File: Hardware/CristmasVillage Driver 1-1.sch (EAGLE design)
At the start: 53 parts, among them CN1 MJ-180SMT, CN2-PROG JST-6PSPI-SIDE-S6B, CN3-SERIAL JST-4PSIDE-S4B, CN5-LEDSTRIPS HDR_2X10_SIDE-MOUNT, IC1 UA78M05DCY, IC2 LM358D, IC3 LM358D, IC4 LM358D, IC5 ATTINY-4/5/9/10, IC6 TINY2313-*S*, Q1 Si2309CD, Q10 NX7002AKW, Q11 NX7002AKW, Q12 NX7002AKW, Q2 NX7002AKW, Q3 NX7002AKW, Q4 NX7002AKW, Q5 NX7002AKW, Q6 NX7002AKW, Q7 NX7002AKW, Q8 NX7002AKW, Q9 NX7002AKW, SW1 POWER, SW2 NIGHT-MODE

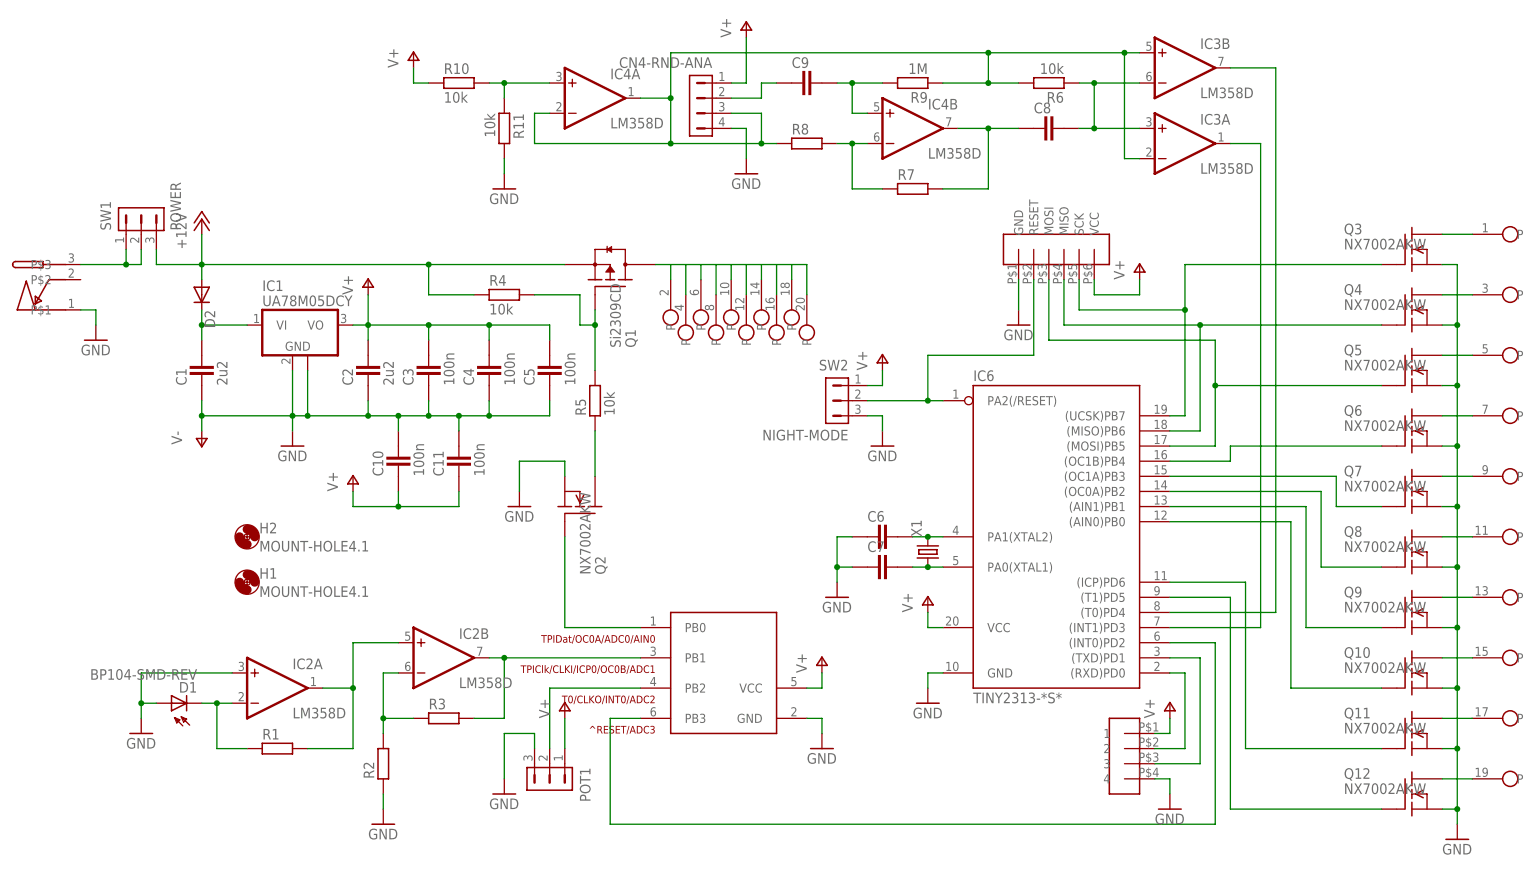
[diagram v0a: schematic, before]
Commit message: Changed from FM tuned antenna idea to Zener Noise for random: v1.1
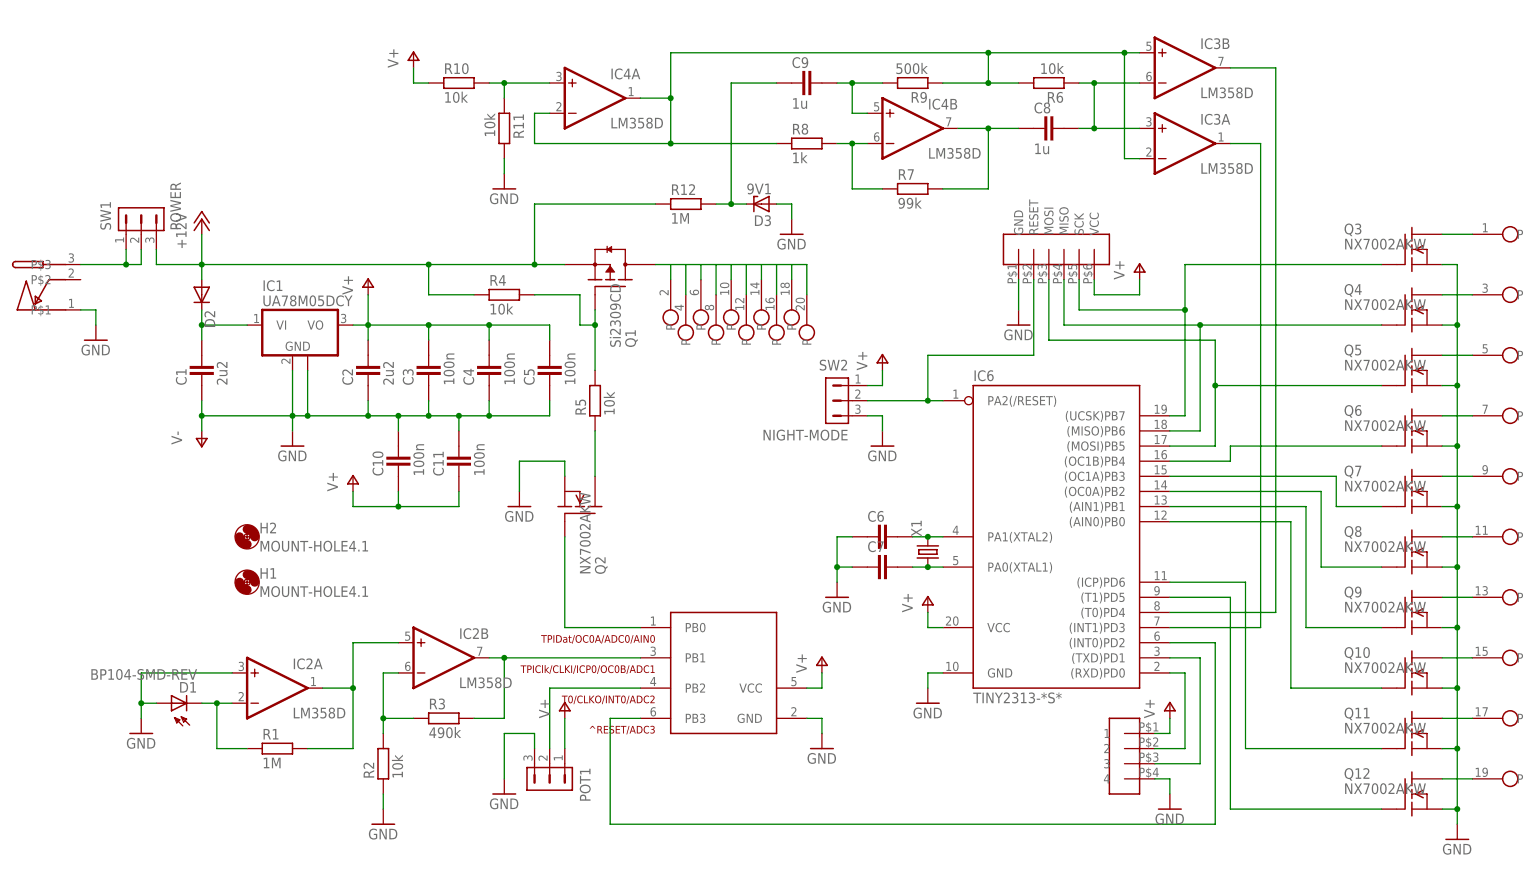
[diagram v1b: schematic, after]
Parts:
- removed CN4-RND-ANA: (no value), con-hdrs40:HDR-1X4-SIP-100
- added D3: 9V1, diode:ZENER-DIODESOT23
- added R12: 1M, ipc-7351-resistor:RESISTOR_0603
- C8, C9: value (none) -> 1u
- R1: value (none) -> 1M
- R2: value (none) -> 10k
- R3: value (none) -> 490k
- R7: value (none) -> 99k
- R8: value (none) -> 1k
- R9: value 1M -> 500k
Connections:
- removed net RANDOM-ANALOG-SIG: C9.1, CN4-RND-ANA.2
- new net N$42: C9.1, D3.C, R12.2
- net +12V: now also R12.1
- net GND: now also D3.A; no longer CN4-RND-ANA.4
- net HALF-VCC: no longer CN4-RND-ANA.3
- net V+: no longer CN4-RND-ANA.1
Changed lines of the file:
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@@
 <part name="GND3" library="supply1" deviceset="GND" device=""/>
 <part name="C3" library="ipc-7351-capacitor" deviceset="CAPACITOR_" device="0603" value="100n"/>
-<part name="R1" library="ipc-7351-resistor" deviceset="RESISTOR_" device="0603"/>
+<part name="R1" library="ipc-7351-resistor" deviceset="RESISTOR_" device="0603" value="1M"/>
 <part name="Q1" library="ipc-7351-transistor" deviceset="MOSFET-PCH_" device="SOT-23" value="Si2309CD"/>
-<part name="R2" library="ipc-7351-resistor" deviceset="RESISTOR_" device="0603"/>
-<part name="R3" library="ipc-7351-resistor" deviceset="RESISTOR_" device="0603"/>
+<part name="R2" library="ipc-7351-resistor" deviceset="RESISTOR_" device="0603" value="10k"/>
+<part name="R3" library="ipc-7351-resistor" deviceset="RESISTOR_" device="0603" value="490k"/>
 <part name="GND4" library="supply1" deviceset="GND" device=""/>
 <part name="IC5" library="avr-6" deviceset="ATTINY-4/5/9/10" device=""/>
@@
 <part name="P+8" library="supply1" deviceset="V+" device=""/>
 <part name="GND13" library="supply1" deviceset="GND" device=""/>
-<part name="C8" library="ipc-7351-capacitor" deviceset="CAPACITOR_" device="1206"/>
-<part name="C9" library="ipc-7351-capacitor" deviceset="CAPACITOR_" device="1206"/>
+<part name="C8" library="ipc-7351-capacitor" deviceset="CAPACITOR_" device="1206" value="1u"/>
+<part name="C9" library="ipc-7351-capacitor" deviceset="CAPACITOR_" device="1206" value="1u"/>
 <part name="IC4" library="linear4" deviceset="LM358" device="D"/>
 <part name="R6" library="ipc-7351-resistor" deviceset="RESISTOR_" device="0603" value="10k"/>
-<part name="R7" library="ipc-7351-resistor" deviceset="RESISTOR_" device="0603"/>
-<part name="R8" library="ipc-7351-resistor" deviceset="RESISTOR_" device="0603"/>
-<part name="R9" library="ipc-7351-resistor" deviceset="RESISTOR_" device="0603" value="1M"/>
+<part name="R7" library="ipc-7351-resistor" deviceset="RESISTOR_" device="0603" value="99k"/>
+<part name="R8" library="ipc-7351-resistor" deviceset="RESISTOR_" device="0603" value="1k"/>
+<part name="R9" library="ipc-7351-resistor" deviceset="RESISTOR_" device="0603" value="500k"/>
 <part name="R10" library="ipc-7351-resistor" deviceset="RESISTOR_" device="0603" value="10k"/>
 <part name="R11" library="ipc-7351-resistor" deviceset="RESISTOR_" device="0603" value="10k"/>
 <part name="P+9" library="supply1" deviceset="V+" device=""/>
 <part name="GND14" library="supply1" deviceset="GND" device=""/>
-<part name="CN4-RND-ANA" library="con-hdrs40" deviceset="HDR-1X4" device="-SIP-100"/>
-<part name="GND15" library="supply1" deviceset="GND" device=""/>
-<part name="P+10" library="supply1" deviceset="V+" device=""/>
 <part name="H1" library="holes" deviceset="MOUNT-HOLE" device="4.1"/>
 <part name="H2" library="holes" deviceset="MOUNT-HOLE" device="4.1"/>
@@
 <part name="C11" library="ipc-7351-capacitor" deviceset="CAPACITOR_" device="0603" value="100n"/>
 <part name="P+11" library="supply1" deviceset="V+" device=""/>
+<part name="D3" library="diode" deviceset="ZENER-DIODE" device="SOT23" value="9V1"/>
+<part name="R12" library="ipc-7351-resistor" deviceset="RESISTOR_" device="0603" value="1M"/>
+<part name="GND15" library="supply1" deviceset="GND" device=""/>
 </parts>
 <sheets>
@@
 <instance part="P+9" gate="1" x="68.58" y="137.16"/>
 <instance part="GND14" gate="1" x="83.82" y="114.3"/>
-<instance part="CN4-RND-ANA" gate="G$1" x="116.84" y="129.54" rot="MR0"/>
-<instance part="GND15" gate="1" x="124.46" y="116.84"/>
-<instance part="P+10" gate="1" x="124.46" y="142.24"/>
 <instance part="H1" gate="G$1" x="40.64" y="48.26"/>
 <instance part="H2" gate="G$1" x="40.64" y="55.88"/>
@@
 <instance part="C11" gate="G$1" x="76.2" y="68.58" rot="R90"/>
 <instance part="P+11" gate="1" x="58.42" y="66.04"/>
+<instance part="D3" gate="G$1" x="127" y="111.76" rot="R180"/>
+<instance part="R12" gate="G$1" x="114.3" y="111.76"/>
+<instance part="GND15" gate="1" x="132.08" y="106.68"/>
 </instances>
 <busses>
@@
 </segment>
 <segment>
-<pinref part="CN4-RND-ANA" gate="G$1" pin="4"/>
+<pinref part="D3" gate="G$1" pin="A"/>
 <pinref part="GND15" gate="1" pin="GND"/>
-<wire x1="121.92" y1="124.46" x2="124.46" y2="124.46" width="0.1524" layer="91"/>
-<wire x1="124.46" y1="124.46" x2="124.46" y2="119.38" width="0.1524" layer="91"/>
+<wire x1="129.54" y1="111.76" x2="132.08" y2="111.76" width="0.1524" layer="91"/>
+<wire x1="132.08" y1="111.76" x2="132.08" y2="109.22" width="0.1524" layer="91"/>
 </segment>
 </net>
@@
 </segment>
 <segment>
-<pinref part="CN4-RND-ANA" gate="G$1" pin="1"/>
-<pinref part="P+10" gate="1" pin="V+"/>
-<wire x1="121.92" y1="132.08" x2="124.46" y2="132.08" width="0.1524" layer="91"/>
-<wire x1="124.46" y1="132.08" x2="124.46" y2="139.7" width="0.1524" layer="91"/>
-</segment>
-<segment>
 <pinref part="P+11" gate="1" pin="V+"/>
 <wire x1="58.42" y1="63.5" x2="58.42" y2="60.96" width="0.1524" layer="91"/>
@@
 <junction x="33.02" y="101.6"/>
 <pinref part="Q1" gate="G$1" pin="S"/>
-<wire x1="93.98" y1="101.6" x2="71.12" y2="101.6" width="0.1524" layer="91"/>
+<wire x1="93.98" y1="101.6" x2="88.9" y2="101.6" width="0.1524" layer="91"/>
 <pinref part="SW1" gate="G$1" pin="3"/>
+<wire x1="88.9" y1="101.6" x2="71.12" y2="101.6" width="0.1524" layer="91"/>
 <wire x1="71.12" y1="101.6" x2="33.02" y2="101.6" width="0.1524" layer="91"/>
 <wire x1="25.4" y1="104.14" x2="25.4" y2="101.6" width="0.1524" layer="91"/>
@@
 <wire x1="71.12" y1="96.52" x2="71.12" y2="101.6" width="0.1524" layer="91"/>
 <junction x="71.12" y="101.6"/>
+<pinref part="R12" gate="G$1" pin="1"/>
+<wire x1="109.22" y1="111.76" x2="88.9" y2="111.76" width="0.1524" layer="91"/>
+<wire x1="88.9" y1="111.76" x2="88.9" y2="101.6" width="0.1524" layer="91"/>
+<junction x="88.9" y="101.6"/>
 </segment>
 </net>
@@
 <wire x1="111.76" y1="129.54" x2="106.68" y2="129.54" width="0.1524" layer="91"/>
 <pinref part="R8" gate="G$1" pin="1"/>
-<wire x1="129.54" y1="121.92" x2="127" y2="121.92" width="0.1524" layer="91"/>
-<wire x1="127" y1="121.92" x2="111.76" y2="121.92" width="0.1524" layer="91"/>
+<wire x1="129.54" y1="121.92" x2="111.76" y2="121.92" width="0.1524" layer="91"/>
 <wire x1="111.76" y1="129.54" x2="111.76" y2="137.16" width="0.1524" layer="91"/>
 <pinref part="IC3" gate="A" pin="-IN"/>
@@
 <junction x="165.1" y="137.16"/>
 <junction x="111.76" y="121.92"/>
-<wire x1="127" y1="127" x2="127" y2="121.92" width="0.1524" layer="91"/>
-<junction x="127" y="121.92"/>
-<pinref part="CN4-RND-ANA" gate="G$1" pin="3"/>
-<wire x1="127" y1="127" x2="121.92" y2="127" width="0.1524" layer="91"/>
 </segment>
 </net>
@@
 </segment>
 </net>
-<net name="RANDOM-ANALOG-SIG" class="0">
-<segment>
-<wire x1="127" y1="129.54" x2="127" y2="132.08" width="0.1524" layer="91"/>
+<net name="N$42" class="0">
+<segment>
+<pinref part="R12" gate="G$1" pin="2"/>
+<pinref part="D3" gate="G$1" pin="C"/>
+<wire x1="119.38" y1="111.76" x2="121.92" y2="111.76" width="0.1524" layer="91"/>
+<wire x1="121.92" y1="111.76" x2="124.46" y2="111.76" width="0.1524" layer="91"/>
+<wire x1="121.92" y1="111.76" x2="121.92" y2="132.08" width="0.1524" layer="91"/>
 <pinref part="C9" gate="G$1" pin="1"/>
-<wire x1="127" y1="132.08" x2="129.54" y2="132.08" width="0.1524" layer="91"/>
-<pinref part="CN4-RND-ANA" gate="G$1" pin="2"/>
-<wire x1="127" y1="129.54" x2="121.92" y2="129.54" width="0.1524" layer="91"/>
-</segment>
-</net>
+<wire x1="121.92" y1="132.08" x2="129.54" y2="132.08" width="0.1524" layer="91"/>
+<junction x="121.92" y="111.76"/>
+</segment>
+</net>
